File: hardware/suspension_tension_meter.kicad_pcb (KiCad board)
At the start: 2 copper layers, 77 x 47 mm, 72 parts, among them J1 Conn_01x04, J2 Conn_01x06, J3 Conn_01x04, J4 Conn_01x04, J5 Terminator, SW1 Tactswitch, U1 STM32L4P5RET6, U2 AOZ1280CI, U3 LM1117-5.0, U4 LM1117-3.3, U5 ATA6561-GAQW-N, U6 NAU7802SGI, U7 NAU7802SGI, Y1 16MHz

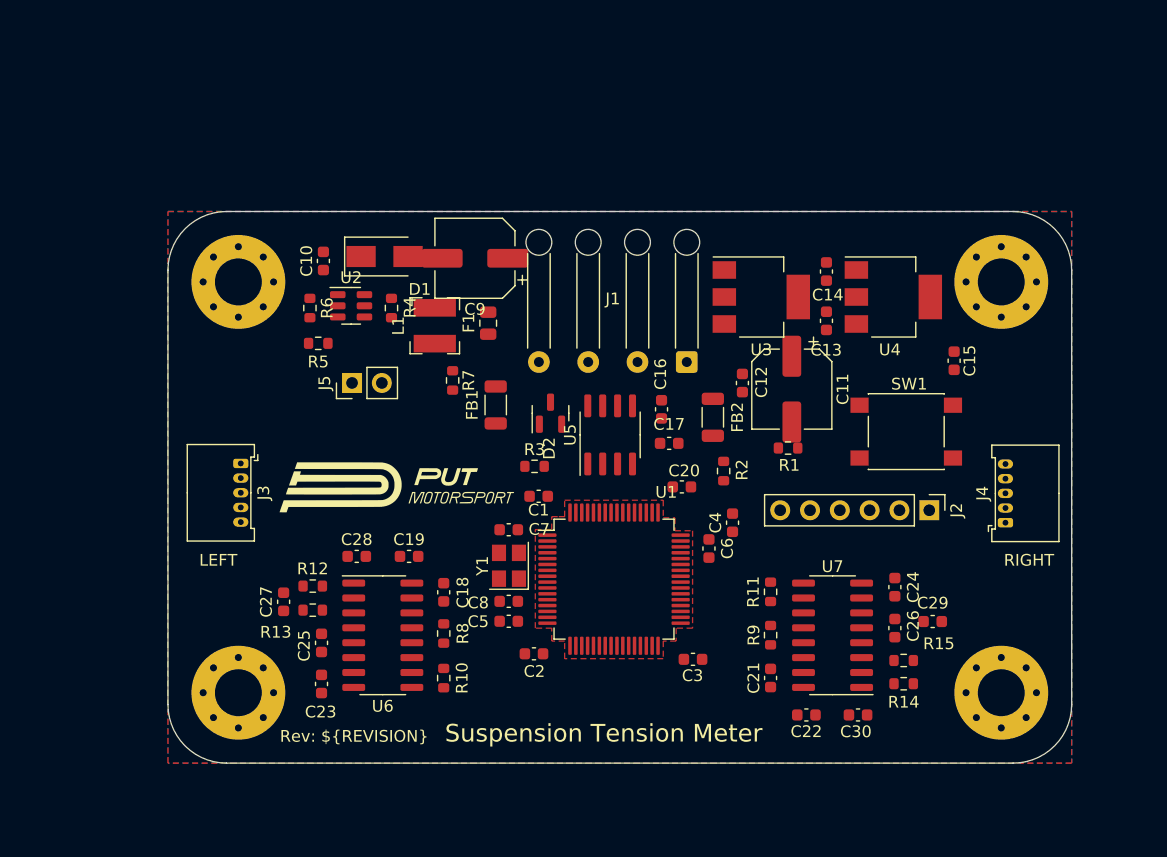
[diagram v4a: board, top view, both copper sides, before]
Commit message: Route PCB tracks
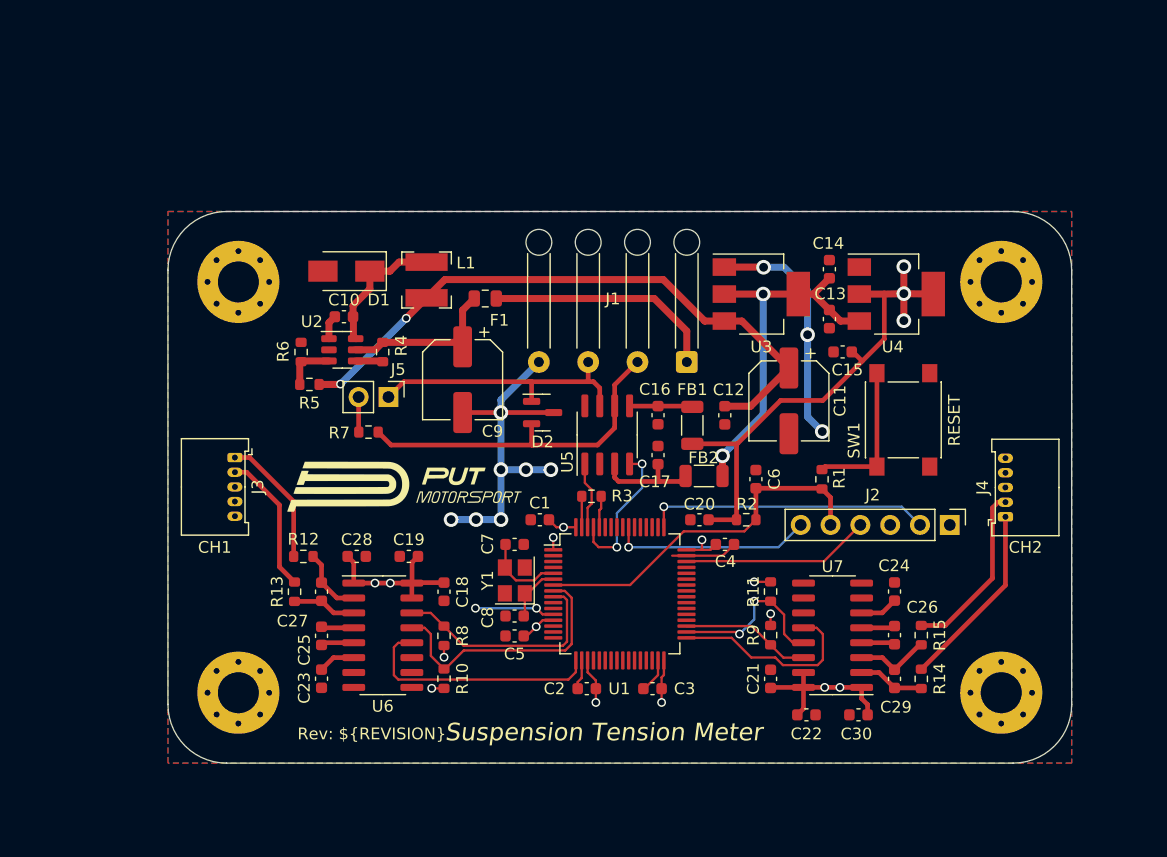
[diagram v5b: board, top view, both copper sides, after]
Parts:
- removed the G*** at (131.0, 113.0)
- removed the REF** at (115.0, 85.0)
- removed the REF** at (180.0, 85.0)
- removed the REF** at (180.0, 120.0)
- removed the REF** at (115.0, 120.0)
- added REF**: MountingHole_3.5mm_Pad_Via, MountingHole:MountingHole_3.5mm_Pad_Via, F.Cu at (115.0, 120.0)
- added REF**: MountingHole_3.5mm_Pad_Via, MountingHole:MountingHole_3.5mm_Pad_Via, F.Cu at (180.0, 85.0)
- added REF**: MountingHole_3.5mm_Pad_Via, MountingHole:MountingHole_3.5mm_Pad_Via, F.Cu at (115.0, 85.0)
- added REF**: MountingHole_3.5mm_Pad_Via, MountingHole:MountingHole_3.5mm_Pad_Via, F.Cu at (180.0, 120.0)
- C9: value 4.7μF -> 10μF
- moved FB1 16.8 mm to (153.6, 97.3)
- moved G*** 10.6 mm to (147.2, 118.4)
- moved C9 10.4 mm to (134.1, 93.4), turned to -90 degrees
- moved C15 9.53 mm to (166.4, 91.0), turned to 180 degrees
- moved R7 8.41 mm to (126.0, 97.8), turned to 0 degrees
- moved C6 7.14 mm to (159.1, 101.8)
- moved C29 5.87 mm to (170.9, 118.9), turned to 90 degrees
- moved R3 5.48 mm to (145.1, 103.3)
- moved C2 5.39 mm to (144.7, 119.7), turned to 180 degrees
- moved C10 5.06 mm to (124.0, 88.0), turned to 0 degrees
- moved FB2 5.06 mm to (154.6, 101.6), turned to 180 degrees
- moved R2 4.57 mm to (158.2, 105.3), turned to 0 degrees
- moved C3 4.26 mm to (150.2, 119.7), turned to 180 degrees
- moved L1 3.96 mm to (131.0, 84.9)
- moved R1 3.93 mm to (164.7, 101.8), turned to 90 degrees
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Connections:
- J1 pad 2: /CAN+ -> /CAN-
- J1 pad 3: /CAN- -> /CAN+
- U1 pad 10: /DRDY1 -> unconnected-(U1-Pad10)
- U1 pad 17: unconnected-(U1-Pad17) -> /DRDY1
- U1 pad 33: unconnected-(U1-Pad33) -> /DRDY2
- U1 pad 36: /DRDY2 -> unconnected-(U1-Pad36)
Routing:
- net +3.3V: track 0.00 -> 95.2 mm, vias 0 -> 17
- net GND: track 0.00 -> 72.2 mm, vias 0 -> 12
- net /Power Supply/6.42V: track 0.00 -> 53.7 mm, vias 0 -> 2
- net +5V: track 0.00 -> 31.3 mm, vias 0 -> 2
- net /NRST: track 0.00 -> 31.3 mm
- net /CAN-: track 0.00 -> 29.5 mm
- net /SWCLK: track 0.00 -> 24.2 mm, vias 0 -> 1
- net /CAN+: track 0.00 -> 23.7 mm
- net /SCLK1: track 0.00 -> 22.8 mm
- net /DRDY1: track 0.00 -> 21.0 mm
- net /PWR+: track 0.00 -> 20.0 mm
- net /SDIO1: track 0.00 -> 19.4 mm
- net /SWO: track 0.00 -> 17.2 mm, vias 0 -> 1
- net /DRDY2: track 0.00 -> 16.8 mm
- net /SWDIO: track 0.00 -> 16.1 mm
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- added copper zone on B.Cu, net +3.3V
- removed copper zone on F.Cu, net +3.3V
- removed copper zone on B.Cu, net GND
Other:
- board text added: "CH1"
- board text added: "CH2"
- board text added: "Ignacy Kajdan github.com/ikajdan"
- board text added: "RESET"
- board text removed: "IGNACY KAJDAN github.com/ikajdan"
- board text removed: "LEFT"
- board text removed: "RIGHT"
- board text removed: "‹Per aspera ad astra›"

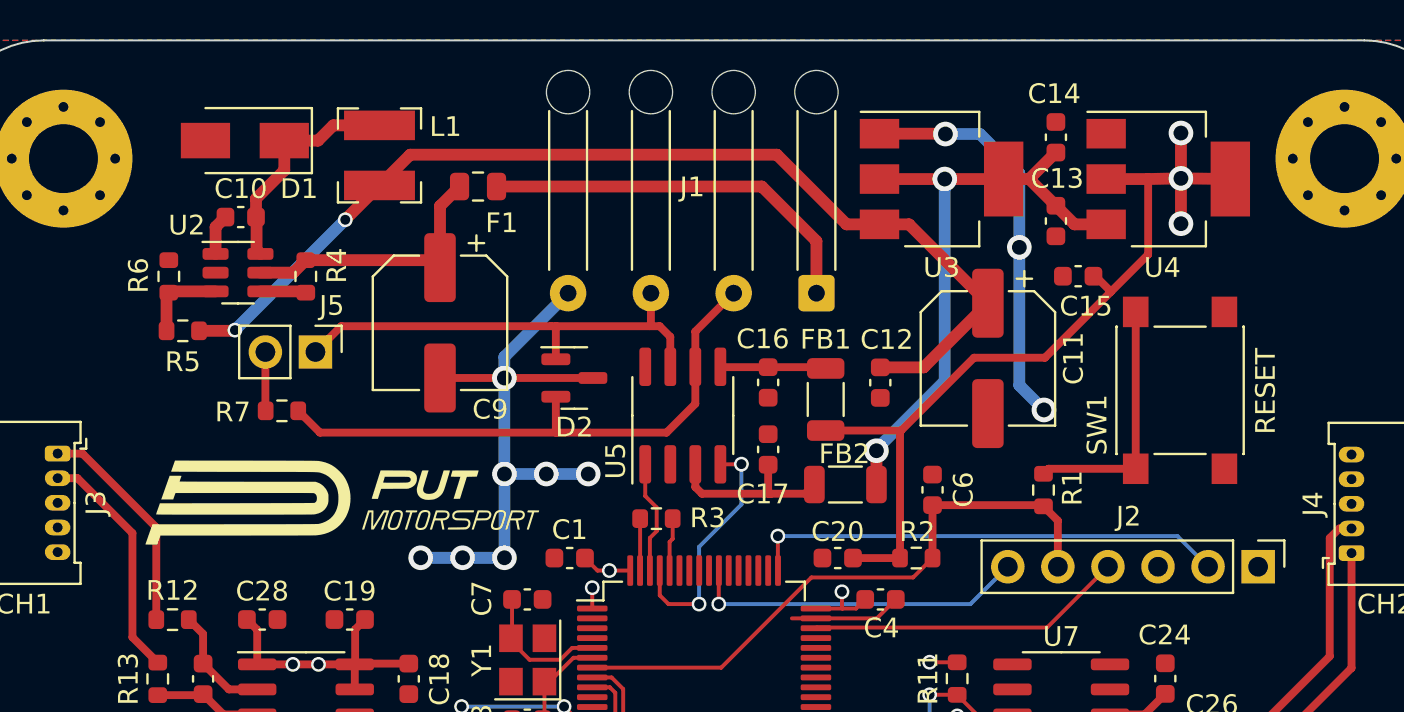
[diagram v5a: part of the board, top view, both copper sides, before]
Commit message: Move input capacitor closer to the converter IC
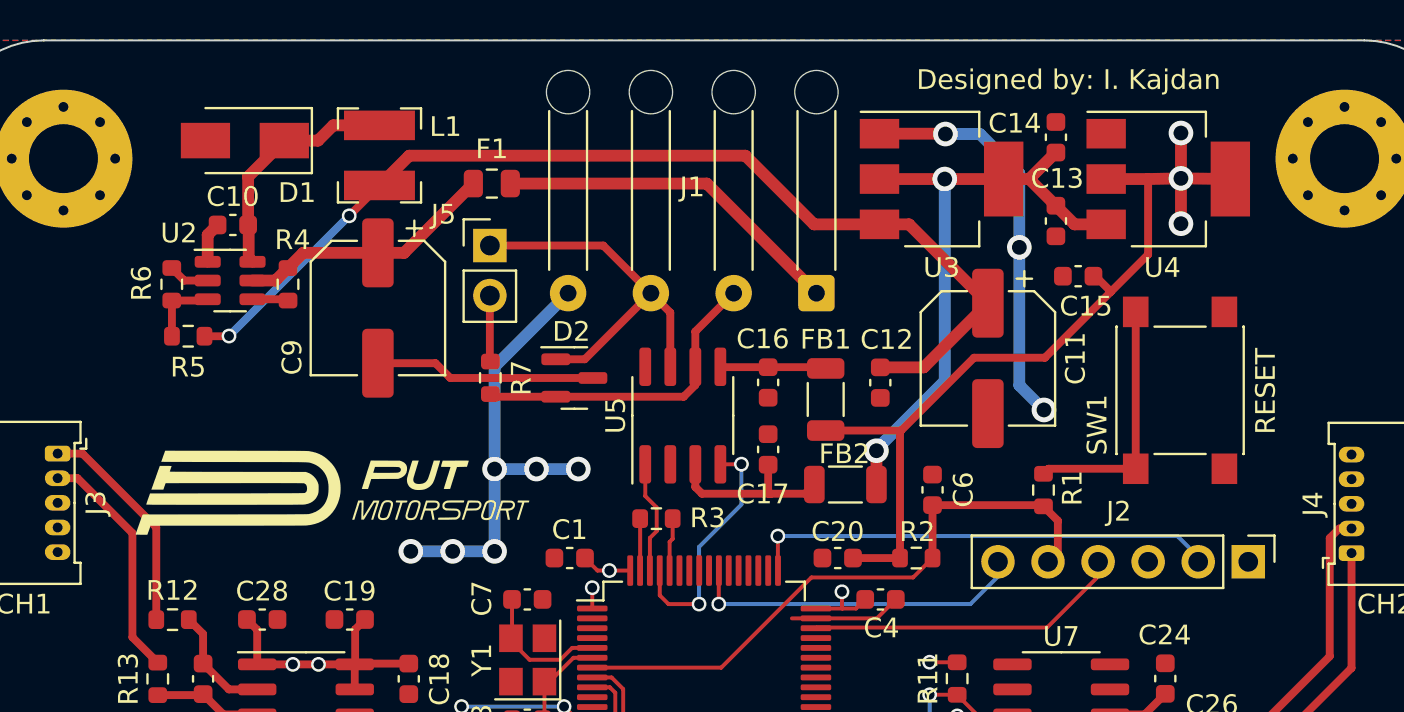
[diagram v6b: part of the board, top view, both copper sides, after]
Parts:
- added G***: LOGO, Local_Library:Susmeter, B.Cu at (147.0, 117.2)
- added G***: LOGO, Local_Library:Sus, B.Cu at (130.4, 115.8)
- moved G*** 16.8 mm to (148.0, 101.6)
- moved R7 10.7 mm to (136.6, 96.2), turned to -90 degrees
- moved J5 10.4 mm to (136.6, 89.4), turned to 0 degrees
- moved C9 3.24 mm to (130.9, 92.6)
- moved R4 0.98 mm to (126.4, 91.4)
- moved F1 0.72 mm to (136.7, 86.3)
- moved G*** 0.71 mm to (128.6, 102.0)
- moved C10 0.57 mm to (123.6, 88.4)
- moved U2 0.57 mm to (123.4, 91.2)
- moved J2 0.56 mm to (175.1, 105.5)
- moved R6 0.43 mm to (120.5, 91.4)
- moved R5 0.39 mm to (121.3, 94.0)
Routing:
- net /CAN-: track 29.5 -> 16.2 mm
- net GND: track 72.2 -> 77.7 mm, vias 12 -> 11
- net /CAN+: track 23.7 -> 19.5 mm
- net /PWR+: track 20.0 -> 17.8 mm
- net Net-(C9-Pad1): track 14.1 -> 13.2 mm
- net /Power Supply/FB: track 4.38 -> 3.66 mm
- net Net-(C10-Pad2): track 11.6 -> 12.2 mm
- net Net-(R4-Pad2): track 2.33 -> 1.83 mm
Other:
- board text added: "Designed by: I. Kajdan"
- board text added: "Ignacy Kajdan"
- board text added: "github.com/ikajdan"
- board text added: "‹Per aspera ad astra›"
- board text removed: "Ignacy Kajdan github.com/ikajdan"

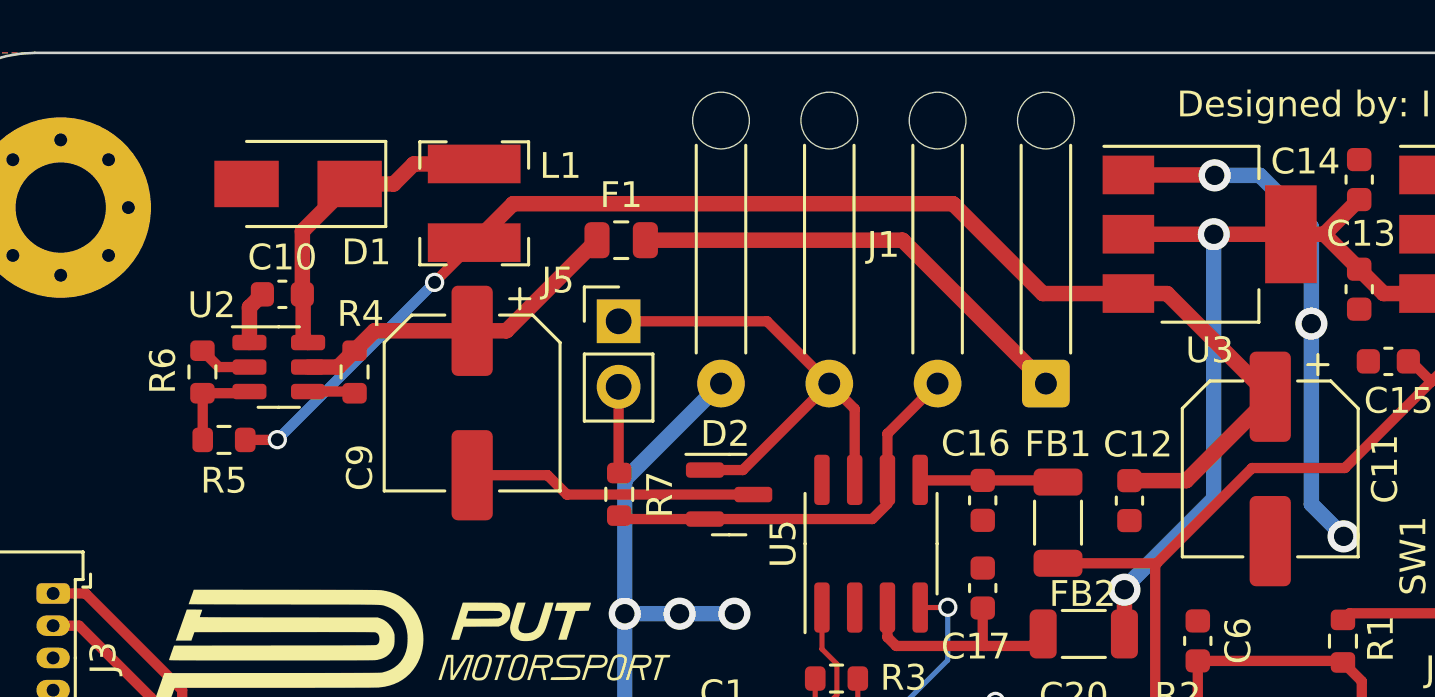
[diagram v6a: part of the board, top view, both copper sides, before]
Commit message: Improve routing around the buck converter
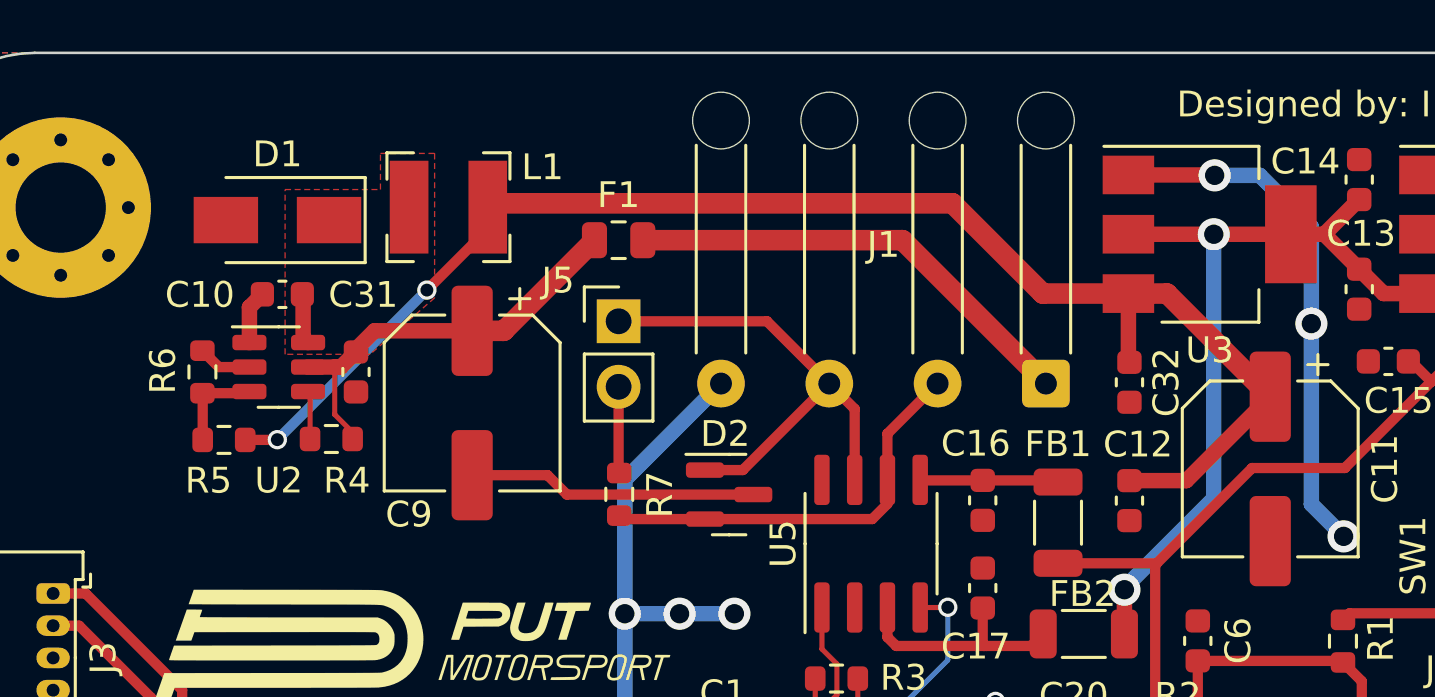
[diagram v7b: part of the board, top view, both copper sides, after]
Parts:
- added C31: 100nF, Capacitor_SMD:C_0603_1608Metric, F.Cu at (126.4, 91.4)
- added C32: 100nF, Capacitor_SMD:C_0603_1608Metric, F.Cu at (156.4, 91.8)
- moved R4 2.75 mm to (125.5, 94.0), turned to 180 degrees
- moved D1 1.61 mm to (123.4, 85.5)
- moved L1 1.01 mm to (130.0, 85.0), turned to 0 degrees
- moved F1 0.10 mm to (136.6, 86.3)
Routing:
- net Net-(C10-Pad2): track 12.2 -> 1.96 mm
- net /Power Supply/6.42V: track 53.5 -> 56.7 mm
- net Net-(C31-Pad1): track 13.2 -> 16.3 mm
- added copper zone on F.Cu, net Net-(C10-Pad2)

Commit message: Release v1.0.0
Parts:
- C13: renamed from C32; value 100nF -> 1μF
- moved G*** 0.50 mm to (130.4, 116.3)
- moved G*** 0.32 mm to (128.4, 101.7)
- renumbered C6 to C1, C9 to C10, C31 to C11, C11 to C12, C12 to C14, C13 to C15, C14 to C16, C15 to C17, C27 to C18, C25 to C19, C7 to C2, C28 to C20, C23 to C21, C18 to C22, C19 to C23, C20 to C24, C21 to C25, C22 to C26, C29 to C27, C26 to C28, C30 to C29, C8 to C3, C24 to C30, C17 to C31, C16 to C32, C1 to C4, C2 to C5, C3 to C6, C4 to C7, C5 to C8, C10 to C9, FB2 to FB1, FB1 to FB2, R2 to R1, R13 to R10, R9 to R11, R11 to R12, R14 to R13, R15 to R14, R7 to R15, R1 to R2, R8 to R7, R10 to R8, R12 to R9, U6 to U5, U7 to U6, U5 to U7
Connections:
- net /PWR+ renamed +24V
- net /Power Supply/6.42V renamed /Power Supply/+6.42V
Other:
- board text added: "CAN Terminator"
- board text added: "CAN+"
- board text added: "CAN-"
- board text added: "GND"
- board text added: "JTAG/SWD"
- board text added: "VCC"
